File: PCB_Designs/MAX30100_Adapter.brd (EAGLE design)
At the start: 19.7 x 25.3 mm, 15 parts

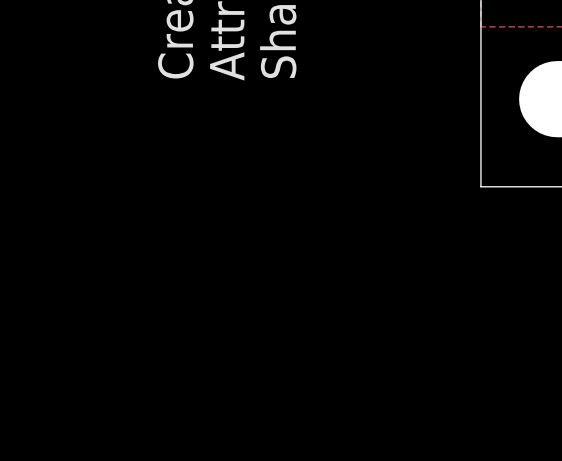
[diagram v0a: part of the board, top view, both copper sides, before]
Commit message: first version of PCB sent to OSHPark
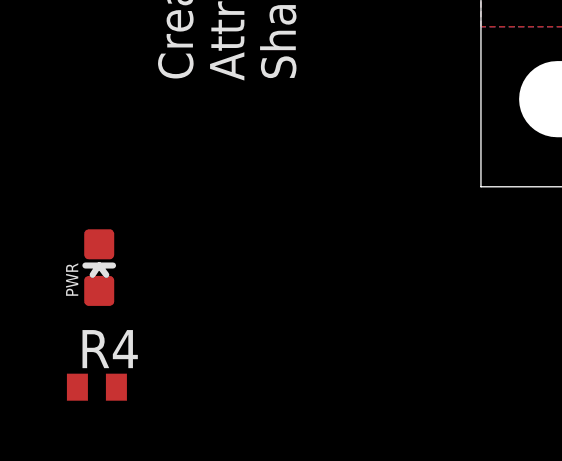
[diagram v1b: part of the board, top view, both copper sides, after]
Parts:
- added PWR: (no value), SparkFun-LED:LED-0603
- added R4: 1k, resistor:R0402
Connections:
- new net N$1: PWR.C, R4.2
- net GND: now also R4.1
- net VCC: now also PWR.A
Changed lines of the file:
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@@
 </element>
 <element name="LOGO1" library="SparkFun-Aesthetics" package="OSHW-LOGO-S" value="OSHW-LOGOS" x="2.3876" y="16.3322" smashed="yes"/>
+<element name="PWR" library="SparkFun-LED" package="LED-0603" value="" x="-12.7254" y="-1.143"/>
+<element name="R4" library="resistor" package="R0402" value="1k" x="-12.8016" y="-5.0292"/>
 </elements>
 <signals>
@@
 <wire x1="6.146784375" y1="15.111475" x2="5.027675" y2="15.111475" width="0.2032" layer="1"/>
 <wire x1="5.027675" y1="15.111475" x2="5.0038" y2="15.0876" width="0.2032" layer="1"/>
+<contactref element="R4" pad="1"/>
+<wire x1="14.602965625" y1="17.631421875" x2="14.847565625" y2="19.44615" width="0" layer="19" extent="1-1"/>
+<wire x1="12.78889375" y1="13.17400625" x2="14.602965625" y2="17.631421875" width="0" layer="19" extent="1-16"/>
+<wire x1="10.63889375" y1="13.97400625" x2="12.78889375" y2="13.17400625" width="0" layer="19" extent="16-16"/>
+<wire x1="8.823103125" y1="11.188403125" x2="10.63889375" y2="13.97400625" width="0" layer="19" extent="1-16"/>
+<wire x1="9.6266" y1="8.3058" x2="7.7978" y2="10.16" width="0" layer="19" extent="1-1"/>
+<wire x1="4.8514" y1="9.525" x2="7.7978" y2="10.16" width="0" layer="19" extent="1-1"/>
+<wire x1="1.6614" y1="10.5306" x2="4.8006" y2="10.9622" width="0" layer="19" extent="1-1"/>
+<wire x1="1.1534" y1="12.2024" x2="1.6002" y2="10.5918" width="0" layer="19" extent="1-1"/>
+<wire x1="14.793975" y1="8.37131875" x2="10.784840625" y2="8.368525" width="0" layer="19" extent="1-1"/>
+<wire x1="5.0038" y1="15.0876" x2="4.8006" y2="10.9622" width="0" layer="19" extent="1-1"/>
+<wire x1="2.140203125" y1="20.49094375" x2="5.027675" y2="15.111475" width="0" layer="19" extent="1-1"/>
+<wire x1="-13.4516" y1="-5.0292" x2="1.6614" y2="9.4234" width="0" layer="19" extent="1-1"/>
 </signal>
 <signal name="N$4">
@@
 <wire x1="9.4742" y1="11.1252" x2="9.4742" y2="10.2108" width="0.2032" layer="16"/>
 <wire x1="9.4742" y1="10.2108" x2="9.4996" y2="10.1854" width="0.2032" layer="16"/>
+<contactref element="PWR" pad="A"/>
+<wire x1="16.256" y1="15.89" x2="16.847565625" y2="19.44615" width="0" layer="19" extent="1-1"/>
+<wire x1="17.526" y1="15.89" x2="16.256" y2="15.89" width="0" layer="19" extent="1-1"/>
+<wire x1="14.602965625" y1="16.331421875" x2="16.256" y2="15.89" width="0" layer="19" extent="1-1"/>
+<wire x1="14.658703125" y1="15.088403125" x2="14.602965625" y2="16.331421875" width="0" layer="19" extent="1-1"/>
+<wire x1="16.30045" y1="10.824196875" x2="14.658703125" y2="15.088403125" width="0" layer="19" extent="1-1"/>
+<wire x1="12.300203125" y1="20.49094375" x2="16.847565625" y2="19.44615" width="0" layer="19" extent="1-1"/>
+<wire x1="10.63889375" y1="12.37400625" x2="14.658703125" y2="15.088403125" width="0" layer="19" extent="1-16"/>
+<wire x1="10.784840625" y1="9.668525" x2="9.4996" y2="10.1854" width="0" layer="19" extent="1-1"/>
+<wire x1="5.7506" y1="10.9622" x2="9.4742" y2="11.1252" width="0" layer="19" extent="1-16"/>
+<wire x1="3.8506" y1="10.9622" x2="5.7506" y2="10.9622" width="0" layer="19" extent="1-1"/>
+<wire x1="2.9614" y1="9.4234" x2="3.8506" y2="10.9622" width="0" layer="19" extent="1-1"/>
+<wire x1="-12.7254" y1="-1.82" x2="2.9614" y2="9.4234" width="0" layer="19" extent="1-1"/>
 </signal>
 <signal name="1.8V">
@@
 <wire x1="9.7536" y1="16.7132" x2="9.8044" y2="16.764" width="0.2032" layer="1"/>
 </signal>
+<signal name="N$1">
+<contactref element="PWR" pad="C"/>
+<contactref element="R4" pad="2"/>
+<wire x1="-12.1516" y1="-5.0292" x2="-12.7254" y2="-0.266" width="0" layer="19" extent="1-1"/>
+</signal>
 </signals>
